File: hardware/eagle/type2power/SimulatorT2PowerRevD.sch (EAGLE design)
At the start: 7 parts

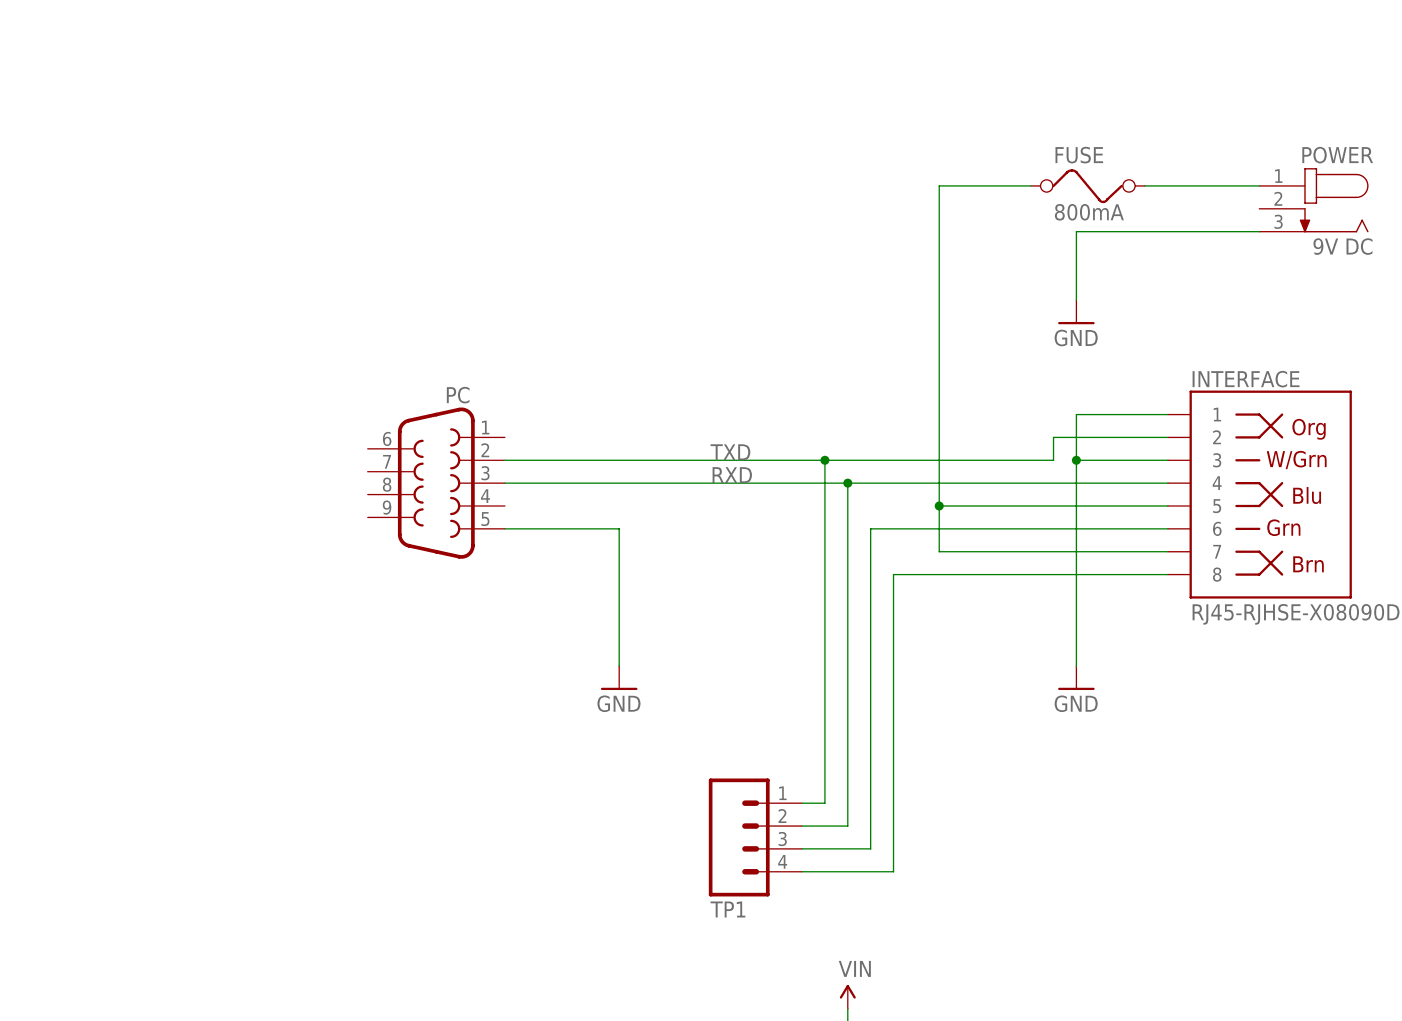
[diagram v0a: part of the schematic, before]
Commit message: Enhanced surge protection
Power Rev D, 2nd PC Rev B boards with improved surge protection,
Gerbers, Cost Estimation tool, New enclosure drilling templates.
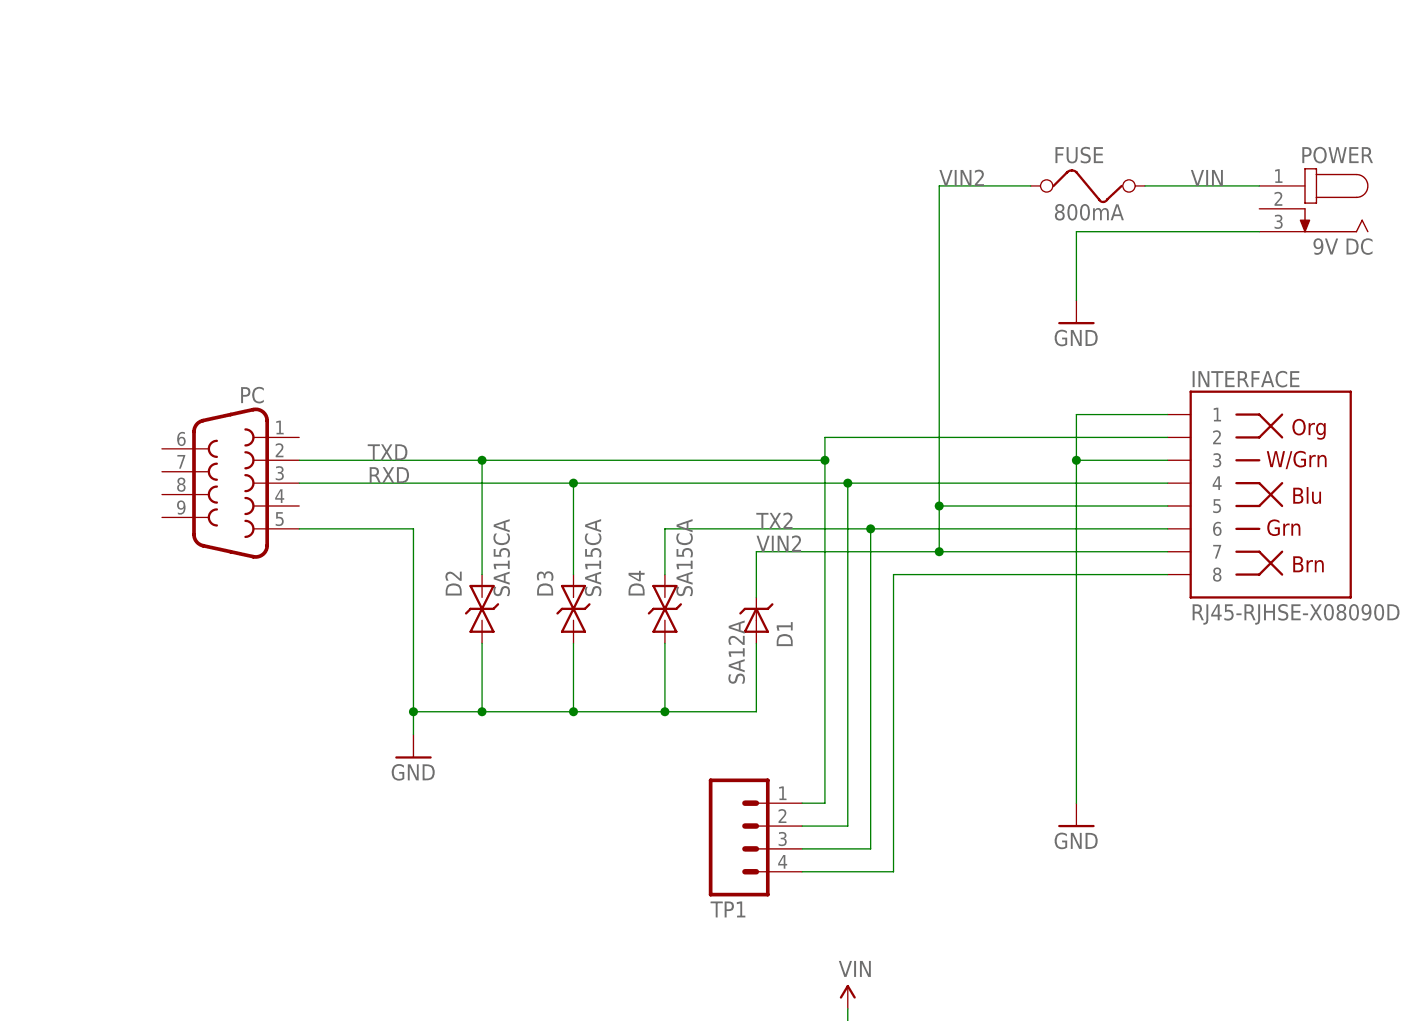
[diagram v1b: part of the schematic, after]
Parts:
- added D1: SA12A, AIC_Custom:SA12A
- added D2, D3, D4: SA15CA, AIC_Custom:SA15CA
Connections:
- net GND: now also D1.ANODE, D2.A, D3.A, D4.A
- net RXD: now also D3.C
- net TX2: now also D4.C
- net TXD: now also D2.C
- net VIN2: now also D1.CATHODE
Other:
- moved on the sheet: PC
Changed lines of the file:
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@@
 <part name="FRAME1" library="SparkFun-Aesthetics" deviceset="FRAME-A4L" device="">
 <attribute name="CNAME" value="Simulator Type 2 Power"/>
-<attribute name="CREVISION" value="Rev C 02/2019"/>
+<attribute name="CREVISION" value="Rev D 07/2019"/>
 <attribute name="DESIGNER" value="A J Instone-Cowie"/>
 </part>
@@
 <part name="GND4" library="SparkFun-Aesthetics" deviceset="GND" device=""/>
 <part name="SUPPLY1" library="SparkFun-Aesthetics" deviceset="VIN" device=""/>
+<part name="D1" library="AIC_Custom" deviceset="SA12A" device=""/>
+<part name="D2" library="AIC_Custom" deviceset="SA15CA" device=""/>
+<part name="D3" library="AIC_Custom" deviceset="SA15CA" device=""/>
+<part name="D4" library="AIC_Custom" deviceset="SA15CA" device=""/>
 </parts>
 <sheets>
@@
 <attribute name="CREVISION" x="5.08" y="5.08" size="1.778" layer="96" display="off"/>
 </instance>
-<instance part="PC" gate="G$1" x="96.52" y="114.3" rot="MR0"/>
+<instance part="PC" gate="G$1" x="73.66" y="114.3" rot="MR0"/>
 <instance part="POWER" gate="G$1" x="193.04" y="144.78" rot="MR0"/>
 <instance part="FUSE" gate="G$1" x="170.18" y="147.32"/>
 <instance part="INTERFACE" gate="JP1" x="185.42" y="114.3"/>
-<instance part="GND1" gate="1" x="167.64" y="91.44"/>
+<instance part="GND1" gate="1" x="167.64" y="76.2"/>
 <instance part="GND2" gate="1" x="167.64" y="132.08"/>
-<instance part="GND3" gate="1" x="116.84" y="91.44"/>
+<instance part="GND3" gate="1" x="93.98" y="83.82"/>
 <instance part="LOGO1" gate="G$1" x="261.62" y="175.26"/>
 <instance part="TP1" gate="G$1" x="132.08" y="76.2" rot="MR180"/>
@@
 <instance part="GND4" gate="1" x="142.24" y="40.64"/>
 <instance part="SUPPLY1" gate="G$1" x="142.24" y="55.88"/>
+<instance part="D1" gate="G$1" x="132.08" y="101.6" rot="R270"/>
+<instance part="D2" gate="G$1" x="101.6" y="99.06" rot="R90"/>
+<instance part="D3" gate="G$1" x="111.76" y="99.06" rot="R90"/>
+<instance part="D4" gate="G$1" x="121.92" y="99.06" rot="R90"/>
 </instances>
 <busses>
@@
 <pinref part="PC" gate="G$1" pin="5"/>
 <pinref part="GND3" gate="1" pin="GND"/>
-<wire x1="104.14" y1="109.22" x2="116.84" y2="109.22" width="0.1524" layer="91"/>
-<wire x1="116.84" y1="109.22" x2="116.84" y2="93.98" width="0.1524" layer="91"/>
+<wire x1="81.28" y1="109.22" x2="93.98" y2="109.22" width="0.1524" layer="91"/>
+<wire x1="93.98" y1="109.22" x2="93.98" y2="88.9" width="0.1524" layer="91"/>
+<pinref part="D2" gate="G$1" pin="A"/>
+<wire x1="93.98" y1="88.9" x2="93.98" y2="86.36" width="0.1524" layer="91"/>
+<wire x1="101.6" y1="96.52" x2="101.6" y2="88.9" width="0.1524" layer="91"/>
+<pinref part="D3" gate="G$1" pin="A"/>
+<wire x1="111.76" y1="96.52" x2="111.76" y2="88.9" width="0.1524" layer="91"/>
+<wire x1="111.76" y1="88.9" x2="101.6" y2="88.9" width="0.1524" layer="91"/>
+<wire x1="101.6" y1="88.9" x2="93.98" y2="88.9" width="0.1524" layer="91"/>
+<junction x="101.6" y="88.9"/>
+<junction x="93.98" y="88.9"/>
+<pinref part="D4" gate="G$1" pin="A"/>
+<wire x1="121.92" y1="96.52" x2="121.92" y2="88.9" width="0.1524" layer="91"/>
+<wire x1="121.92" y1="88.9" x2="111.76" y2="88.9" width="0.1524" layer="91"/>
+<junction x="111.76" y="88.9"/>
+<pinref part="D1" gate="G$1" pin="ANODE"/>
+<wire x1="121.92" y1="88.9" x2="132.08" y2="88.9" width="0.1524" layer="91"/>
+<wire x1="132.08" y1="88.9" x2="132.08" y2="96.52" width="0.1524" layer="91"/>
+<junction x="121.92" y="88.9"/>
 </segment>
 <segment>
 <pinref part="GND1" gate="1" pin="GND"/>
-<wire x1="167.64" y1="93.98" x2="167.64" y2="116.84" width="0.1524" layer="91"/>
 <pinref part="INTERFACE" gate="JP1" pin="1"/>
+<wire x1="167.64" y1="78.74" x2="167.64" y2="116.84" width="0.1524" layer="91"/>
 <wire x1="167.64" y1="116.84" x2="167.64" y2="121.92" width="0.1524" layer="91"/>
 <wire x1="167.64" y1="121.92" x2="177.8" y2="121.92" width="0.1524" layer="91"/>
@@
 <pinref part="FUSE" gate="G$1" pin="2"/>
 <wire x1="187.96" y1="147.32" x2="175.26" y2="147.32" width="0.1524" layer="91"/>
+<label x="180.34" y="147.32" size="1.778" layer="95"/>
 </segment>
 </net>
@@
 <pinref part="PC" gate="G$1" pin="3"/>
 <pinref part="INTERFACE" gate="JP1" pin="4"/>
-<wire x1="104.14" y1="114.3" x2="142.24" y2="114.3" width="0.1524" layer="91"/>
+<wire x1="81.28" y1="114.3" x2="111.76" y2="114.3" width="0.1524" layer="91"/>
 <pinref part="TP1" gate="G$1" pin="2"/>
+<wire x1="111.76" y1="114.3" x2="142.24" y2="114.3" width="0.1524" layer="91"/>
 <wire x1="142.24" y1="114.3" x2="177.8" y2="114.3" width="0.1524" layer="91"/>
 <wire x1="137.16" y1="76.2" x2="142.24" y2="76.2" width="0.1524" layer="91"/>
 <wire x1="142.24" y1="76.2" x2="142.24" y2="114.3" width="0.1524" layer="91"/>
 <junction x="142.24" y="114.3"/>
-<label x="127" y="114.3" size="1.778" layer="95"/>
+<label x="88.9" y="114.3" size="1.778" layer="95"/>
+<pinref part="D3" gate="G$1" pin="C"/>
+<wire x1="111.76" y1="104.14" x2="111.76" y2="114.3" width="0.1524" layer="91"/>
+<junction x="111.76" y="114.3"/>
 </segment>
 </net>
@@
 <segment>
 <pinref part="PC" gate="G$1" pin="2"/>
-<wire x1="104.14" y1="116.84" x2="139.7" y2="116.84" width="0.1524" layer="91"/>
-<wire x1="139.7" y1="116.84" x2="165.1" y2="116.84" width="0.1524" layer="91"/>
-<wire x1="165.1" y1="116.84" x2="165.1" y2="119.38" width="0.1524" layer="91"/>
+<wire x1="81.28" y1="116.84" x2="101.6" y2="116.84" width="0.1524" layer="91"/>
+<wire x1="101.6" y1="116.84" x2="139.7" y2="116.84" width="0.1524" layer="91"/>
+<wire x1="139.7" y1="116.84" x2="139.7" y2="119.38" width="0.1524" layer="91"/>
+<wire x1="139.7" y1="119.38" x2="177.8" y2="119.38" width="0.1524" layer="91"/>
 <pinref part="INTERFACE" gate="JP1" pin="2"/>
-<wire x1="165.1" y1="119.38" x2="177.8" y2="119.38" width="0.1524" layer="91"/>
 <pinref part="TP1" gate="G$1" pin="1"/>
 <wire x1="137.16" y1="78.74" x2="139.7" y2="78.74" width="0.1524" layer="91"/>
 <wire x1="139.7" y1="78.74" x2="139.7" y2="116.84" width="0.1524" layer="91"/>
 <junction x="139.7" y="116.84"/>
-<label x="127" y="116.84" size="1.778" layer="95"/>
+<label x="88.9" y="116.84" size="1.778" layer="95"/>
+<pinref part="D2" gate="G$1" pin="C"/>
+<wire x1="101.6" y1="116.84" x2="101.6" y2="104.14" width="0.1524" layer="91"/>
+<junction x="101.6" y="116.84"/>
 </segment>
 </net>
@@
 <pinref part="INTERFACE" gate="JP1" pin="6"/>
 <wire x1="144.78" y1="109.22" x2="177.8" y2="109.22" width="0.1524" layer="91"/>
+<label x="132.08" y="109.22" size="1.778" layer="95"/>
+<pinref part="D4" gate="G$1" pin="C"/>
+<wire x1="144.78" y1="109.22" x2="121.92" y2="109.22" width="0.1524" layer="91"/>
+<wire x1="121.92" y1="109.22" x2="121.92" y2="104.14" width="0.1524" layer="91"/>
+<junction x="144.78" y="109.22"/>
 </segment>
 </net>
@@
 <wire x1="152.4" y1="106.68" x2="152.4" y2="111.76" width="0.1524" layer="91"/>
 <junction x="152.4" y="111.76"/>
+<label x="152.4" y="147.32" size="1.778" layer="95"/>
+<pinref part="D1" gate="G$1" pin="CATHODE"/>
+<wire x1="132.08" y1="101.6" x2="132.08" y2="106.68" width="0.1524" layer="91"/>
+<wire x1="132.08" y1="106.68" x2="152.4" y2="106.68" width="0.1524" layer="91"/>
+<junction x="152.4" y="106.68"/>
+<label x="132.08" y="106.68" size="1.778" layer="95"/>
 </segment>
 </net>
